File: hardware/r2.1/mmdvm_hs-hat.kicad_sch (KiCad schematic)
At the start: 78 parts, among them P1 OLED, P2 Nextion, P3 SMA, P4 STLink, P5 USB_C_Plug_USB2.0, U1 CC1200, U3 TLV70233_SOT23-5, U4 USBLC6-2, U6 STM32F411CEUx, X1 40MHz, Y1 25MHz

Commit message: Initial routing of r2.1
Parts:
- added JP1: OLED_P1, Jumper:SolderJumper-3_P1.3mm_Bridged2Bar12_RoundedPad1.0x1.5mm, symbol Jumper:Jumper_3_Bridged12
- added JP2: OLED_P2, Jumper:SolderJumper-3_P1.3mm_Bridged2Bar12_RoundedPad1.0x1.5mm, symbol Jumper:Jumper_3_Bridged12
- added R10, R2: 1k, Resistor_SMD:R_0402_1005Metric, symbol Device:R_Small
- added R14: 56k, Resistor_SMD:R_0402_1005Metric, symbol Device:R_Small
- C1, C10, C11, C12, C13, C14, C15, C16, C17, C18, C19, C2, C20, C22, C3, C30, C32, C33, C34, C4, C5, C6, C7, C8, C9: footprint (none) -> Capacitor_SMD:C_0402_1005Metric
- C21, C23, C24, C25, C26, C27, C28: footprint pkl_dipol:C_0402 -> Capacitor_SMD:C_0402_1005Metric
- C31: footprint (none) -> Capacitor_SMD:C_0603_1608Metric
- L1, L2, L3, L4, L6, L7, L8, L9: footprint (none) -> Inductor_SMD:L_0402_1005Metric
- P1, P2, P4: footprint pkl_pin_headers:Pin_Header_Straight_1x04 -> Connector_PinHeader_2.54mm:PinHeader_1x04_P2.54mm_Vertical
- R1, R3, R4, R5, R6, R7, R9: footprint (none) -> Resistor_SMD:R_0402_1005Metric
- R11, R12, R13, R18, R22, R23, R24, R25, R26: footprint pkl_dipol:R_0402 -> Resistor_SMD:R_0402_1005Metric
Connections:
- net NRST is gone; now on net nRST: PI1.40 (GPIO21/SCLK1)
- net +3.3V: now also JP1.1 (A), JP2.3 (B), R10.1, R2.1; no longer P1.1 (Pin_1)
- net CC_MISO: now also U6.16 (PA6)
- net CC_MOSI: now also U6.17 (PA7)
- net CC_SCK: now also U6.15 (PA5)
- net CC_nCS: now also U6.14 (PA4)
- net CC_nRST: now also U6.18 (PB0)
- net COS_LED: now also U6.40 (PB4); no longer U6.4 (PC15)
- net GND: now also JP1.3 (B), JP2.1 (A), R14.1; no longer P1.2 (Pin_2), U1.14 (RBIAS)
- net PTT_LED: now also U6.41 (PB5); no longer U6.3 (PC14)
- net SERVICE: now also U6.39 (PB3); no longer U6.2 (PC13)
- net CC_GPIO0: now reaches U6.25 (PB12)
- net CC_GPIO0: now also U1.10 (GPIO0)
- net CC_GPIO2: now reaches U6.26 (PB13)
- net CC_GPIO2: now also U1.4 (GPIO2)
- net CC_GPIO3: now reaches U6.27 (PB14)
- net CC_GPIO3: now also U1.3 (GPIO3)
- net SCL renamed OLED_SCL
- net OLED_SCL: now also R10.2
- net SDA renamed OLED_SDA
- net OLED_SDA: now also R2.2
- new net: JP1.2 (C), P1.1 (Pin_1)
- new net: JP2.2 (C), P1.2 (Pin_2)
- new net: R14.2, U1.14 (RBIAS)
- no-connect marks 32 -> 29
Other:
- moved on the sheet: AE1, C1, C10, C11, C12, C13, C14, C15, C16, C17, C18, C19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

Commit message: r2.1 RC1
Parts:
- removed P4: STLink, Connector_PinHeader_2.54mm:PinHeader_1x04_P2.54mm_Vertical, symbol Connector_Generic:Conn_01x04
- removed R8: 10k, Resistor_SMD:R_0402_1005Metric, symbol Device:R_Small
- added D5, D6: BAT60A, Diode_SMD:D_SOD-323, symbol Diode:BAT60A
- added P4: STLink, Connector_PinHeader_2.54mm:PinHeader_1x05_P2.54mm_Vertical, symbol Connector_Generic:Conn_01x05
- C27, P1, P2: now not fitted; now left out of the parts list
- P3: footprint Connector_Coaxial:SMA_Amphenol_132291-12_Vertical -> Connector_Coaxial:SMA_Wurth_60312002114503_Vertical; now not fitted; now left out of the parts list
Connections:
- net +3.3V: now also P4.1 (Pin_1)
- net +5V: now also D5.1 (K), D6.1 (K); no longer P5.A4 (VBUS), P5.A9 (VBUS), P5.B4 (VBUS), P5.B9 (VBUS), PI1.2 (5V), PI1.4 (5V), U4.5 (VBUS)
- net BOOT0: now also PI1.38 (GPIO20/MOSI1)
- net GND: now also P4.5 (Pin_5)
- net nRST: now also P4.4 (Pin_4)
- net at U6.34 (PA13): now also P4.2 (Pin_2)
- net at U6.37 (PA14): now also P4.3 (Pin_3)
- new net: D6.2 (A), PI1.2 (5V), PI1.4 (5V)
- new net: D5.2 (A), P5.A4 (VBUS), P5.A9 (VBUS), P5.B4 (VBUS), P5.B9 (VBUS), U4.5 (VBUS)

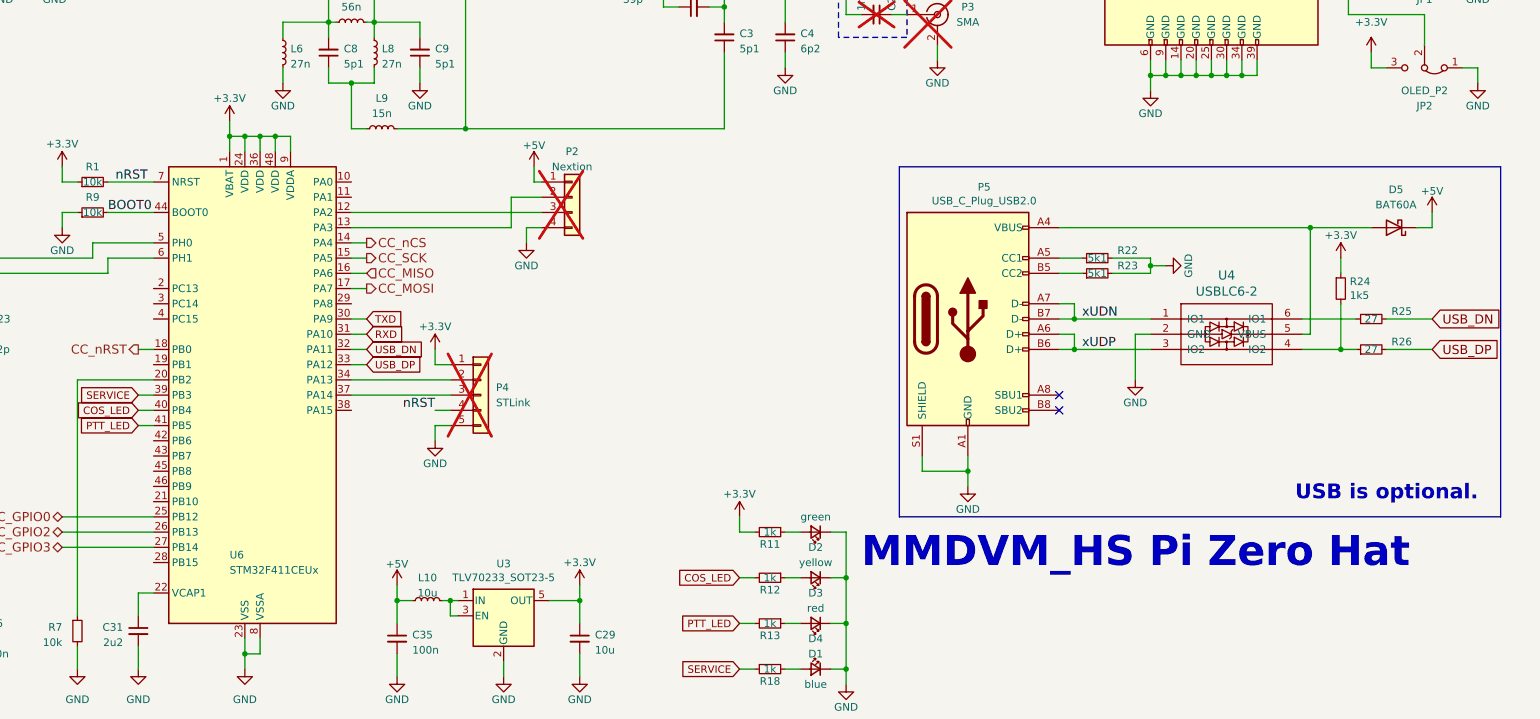
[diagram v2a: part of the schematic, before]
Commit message: r2.1 RC2
Re-worked USB resistors, changed some labels, added vias
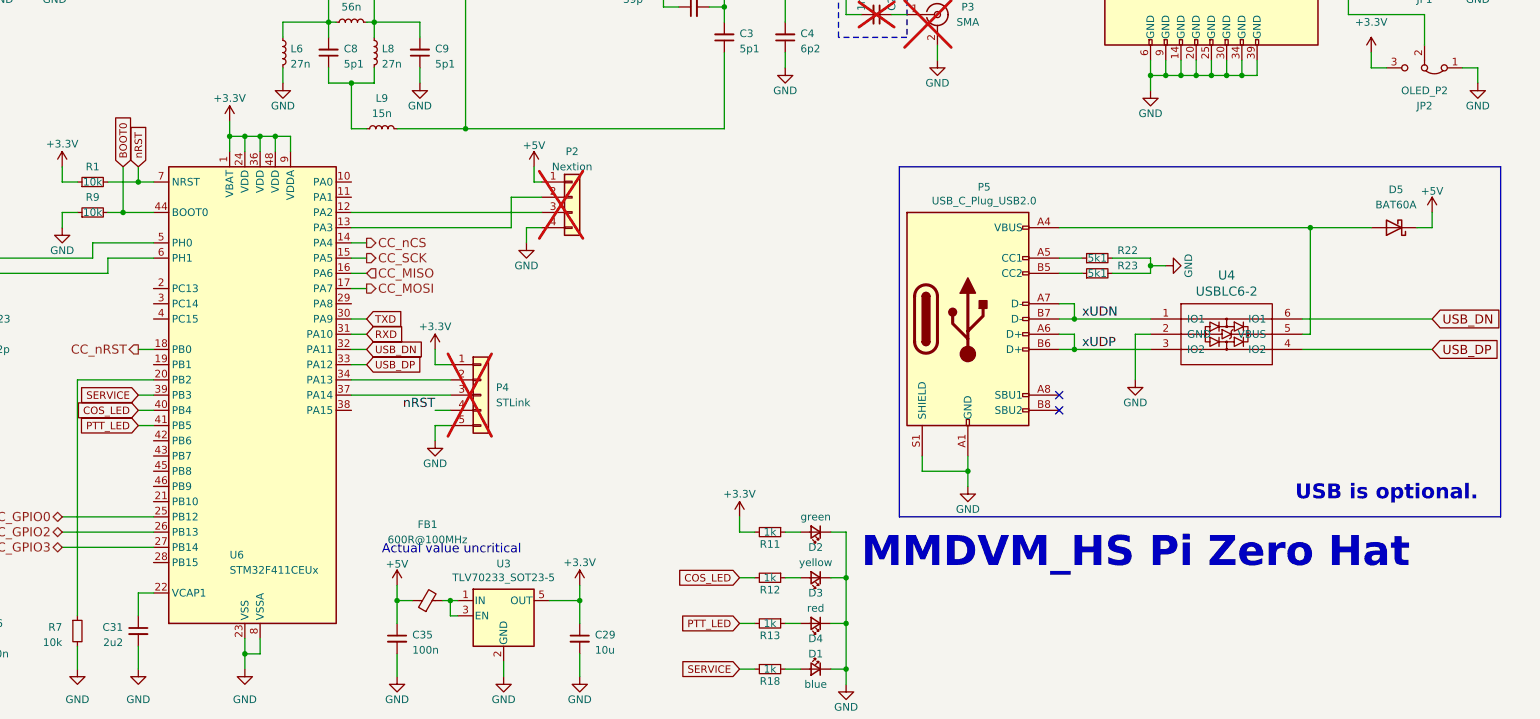
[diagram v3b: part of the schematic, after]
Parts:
- removed R24: 1k5, Resistor_SMD:R_0402_1005Metric, symbol Device:R_Small
- removed R25, R26: 27, Resistor_SMD:R_0402_1005Metric, symbol Device:R_Small
- FB1: renamed from L10; value 10u -> 600R@100MHz; symbol Device:L_Small -> Device:FerriteBead_Small
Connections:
- net USB_DN: now also U4.6 (IO1)
- net USB_DP: now also U4.4 (IO2)
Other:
- note added: "Actual value uncritical"

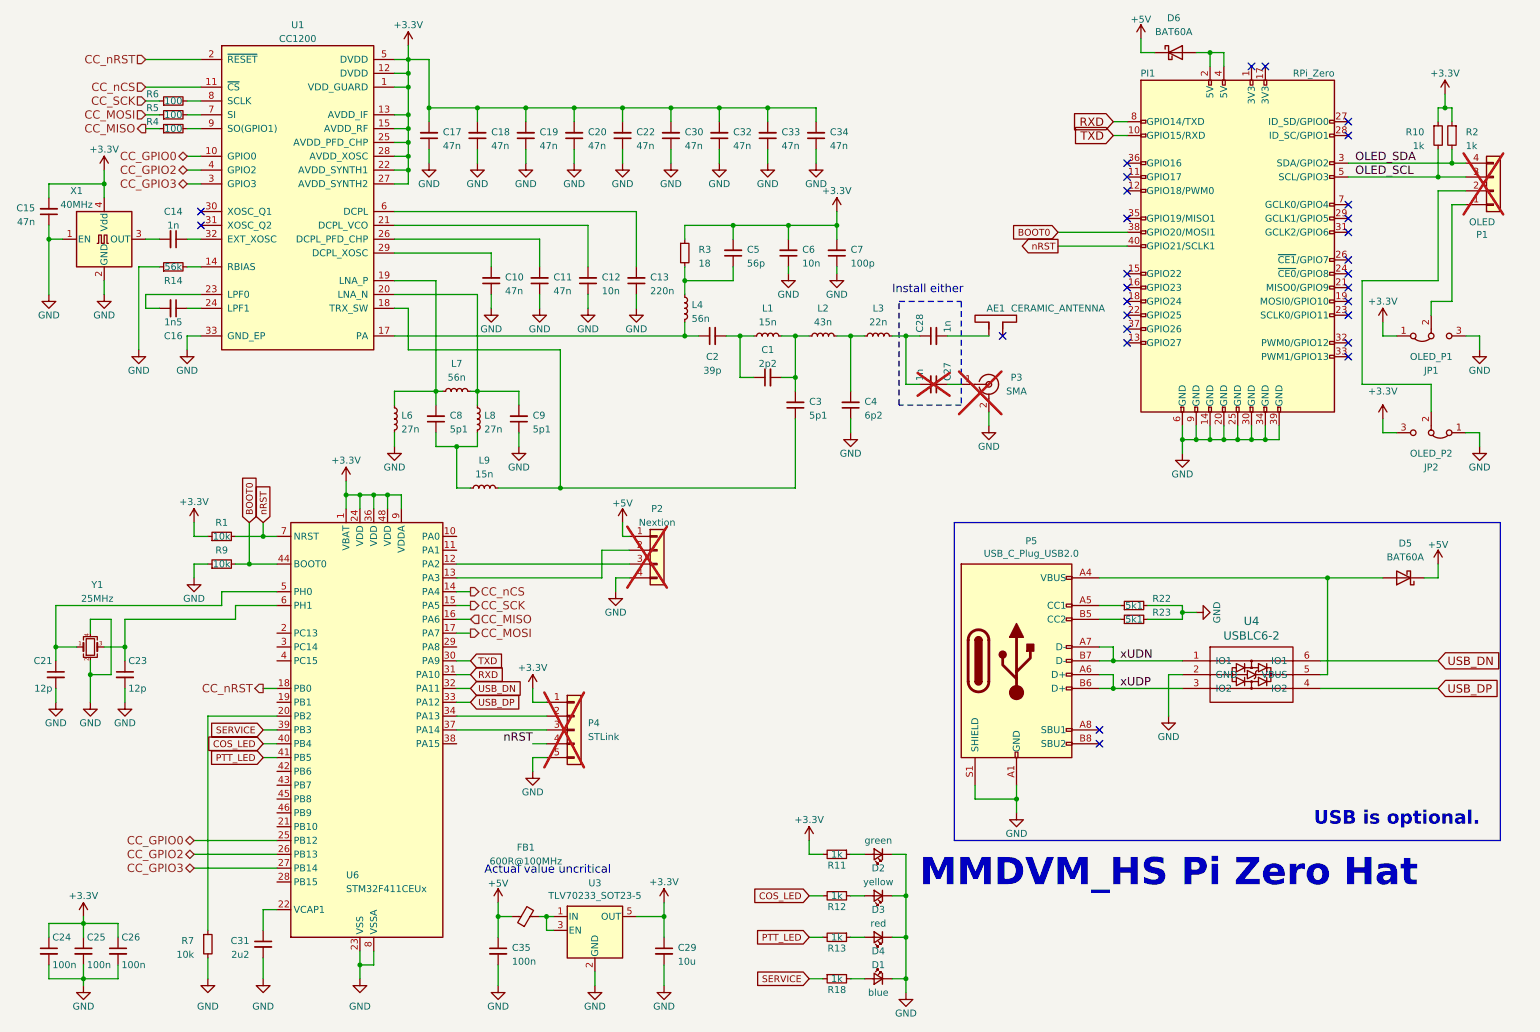
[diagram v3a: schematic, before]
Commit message: Re-annotated symbols
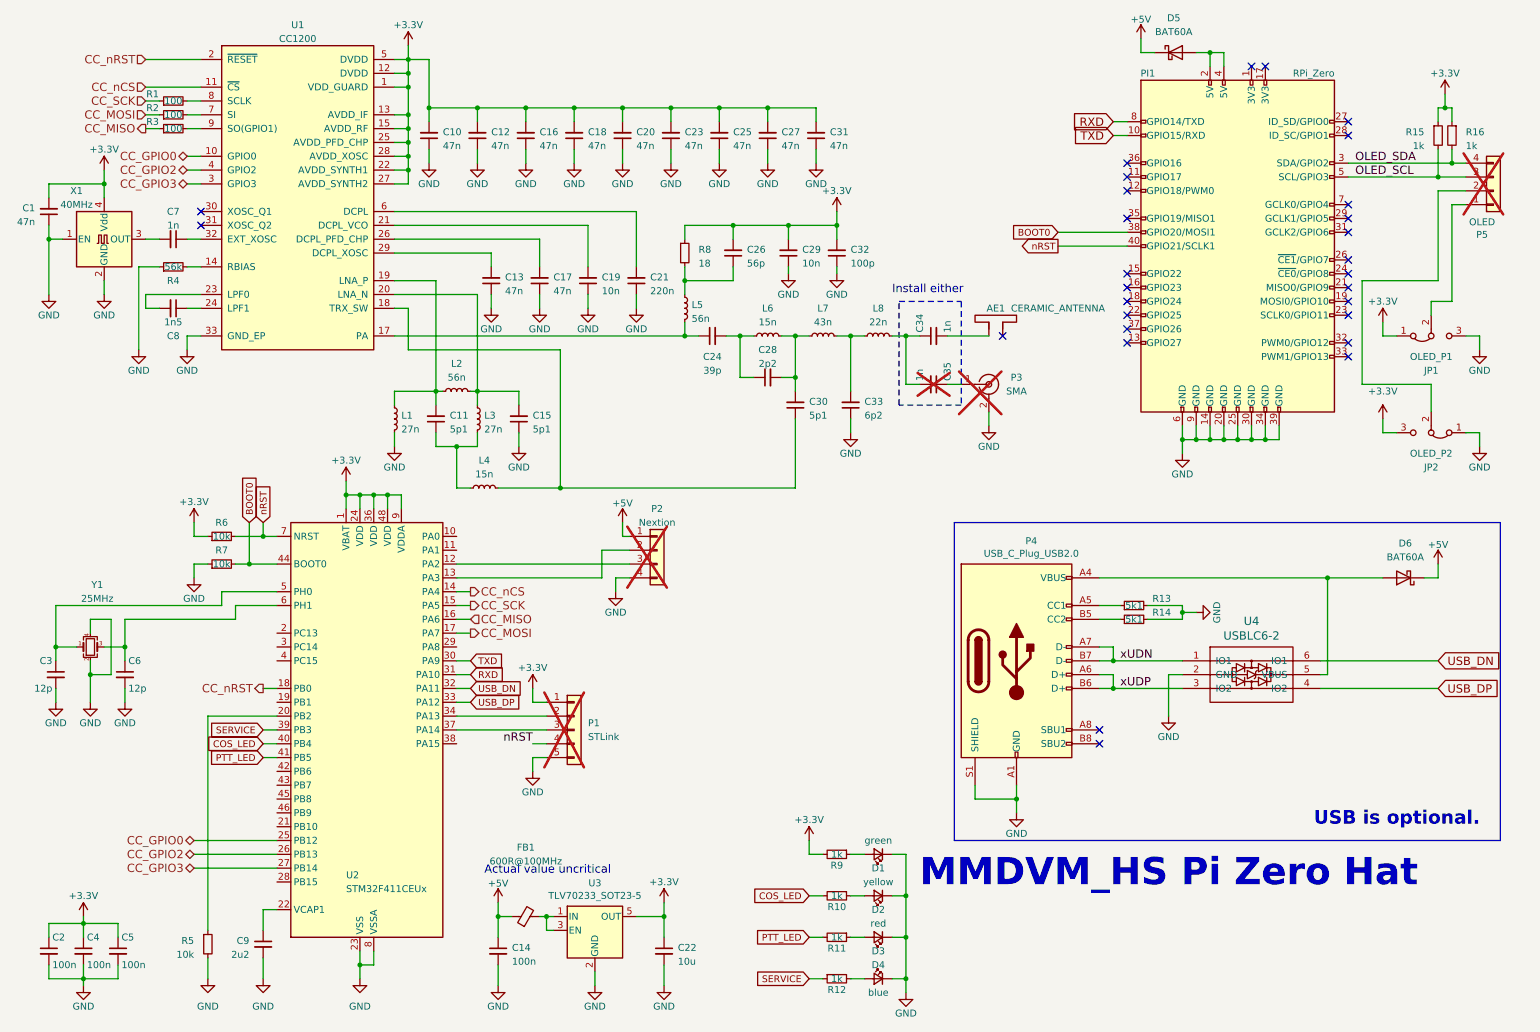
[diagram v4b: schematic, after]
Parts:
- renumbered C15 to C1, C17 to C10, C8 to C11, C18 to C12, C10 to C13, C35 to C14, C9 to C15, C19 to C16, C11 to C17, C20 to C18, C12 to C19, C24 to C2, C22 to C20, C13 to C21, C29 to C22, C30 to C23, C2 to C24, C32 to C25, C5 to C26, C33 to C27, C1 to C28, C6 to C29, C21 to C3, C3 to C30, C34 to C31, C7 to C32, C4 to C33, C28 to C34, C27 to C35, C25 to C4, C26 to C5, C23 to C6, C14 to C7, C16 to C8, C31 to C9, D2 to D1, D3 to D2, D4 to D3, D1 to D4, D6 to D5, D5 to D6, L6 to L1, L7 to L2, L8 to L3, L9 to L4, L4 to L5, L1 to L6, L2 to L7, L3 to L8, P4 to P1, P5 to P4, P1 to P5, R6 to R1, R12 to R10, R13 to R11, R18 to R12, R22 to R13, R23 to R14, R10 to R15, R2 to R16, R5 to R2, R4 to R3, R14 to R4, R7 to R5, R1 to R6, R9 to R7, R3 to R8, R11 to R9, U6 to U2
